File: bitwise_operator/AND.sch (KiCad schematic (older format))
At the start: 4 parts, among them U1 74LS08, U2 74LS08, U3 74LS08, U4 74LS08

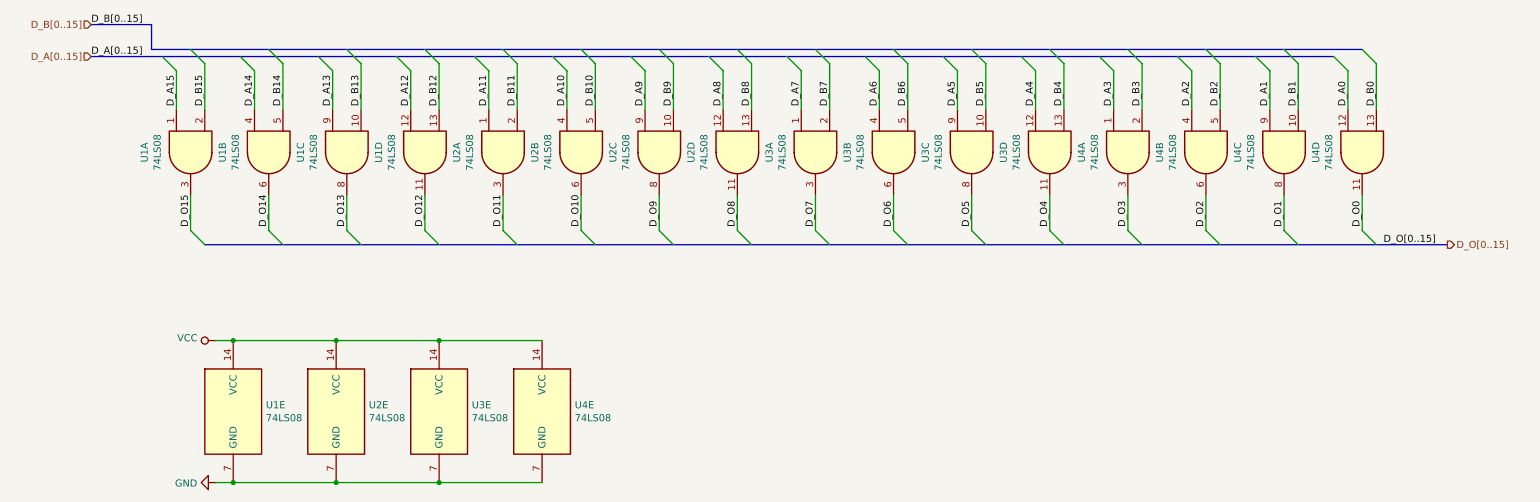
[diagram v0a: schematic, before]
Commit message: add bit operations
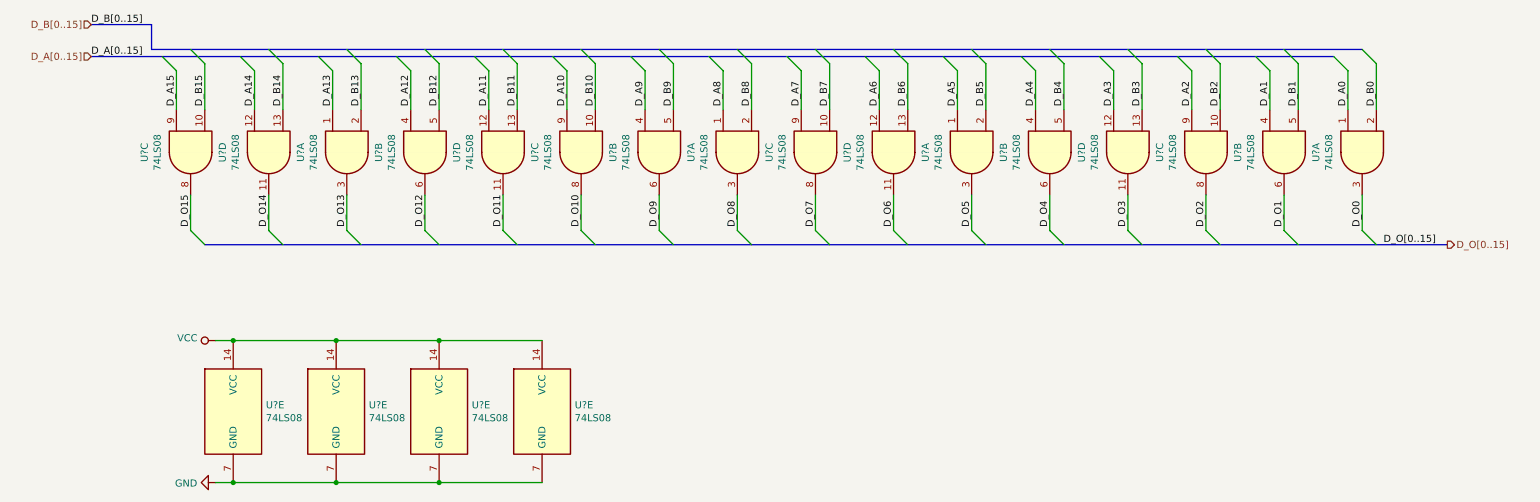
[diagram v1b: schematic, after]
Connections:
- net D_A0: now also U4.1; no longer U4.12
- net D_A1: now also U4.4; no longer U4.9
- net D_A10: now also U2.9; no longer U2.4
- net D_A11: now also U2.12; no longer U2.1
- net D_A12: now also U1.4; no longer U1.12
- net D_A13: now also U1.1; no longer U1.9
- net D_A14: now also U1.12; no longer U1.4
- net D_A15: now also U1.9; no longer U1.1
- net D_A2: now also U4.9; no longer U4.4
- net D_A3: now also U4.12; no longer U4.1
- net D_A4: now also U3.4; no longer U3.12
- net D_A5: now also U3.1; no longer U3.9
- net D_A6: now also U3.12; no longer U3.4
- net D_A7: now also U3.9; no longer U3.1
- net D_A8: now also U2.1; no longer U2.12
- net D_A9: now also U2.4; no longer U2.9
- net D_B0: now also U4.2; no longer U4.13
- net D_B1: now also U4.5; no longer U4.10
- net D_B10: now also U2.10; no longer U2.5
- net D_B11: now also U2.13; no longer U2.2
- net D_B12: now also U1.5; no longer U1.13
- net D_B13: now also U1.2; no longer U1.10
- net D_B14: now also U1.13; no longer U1.5
- net D_B15: now also U1.10; no longer U1.2
- net D_B2: now also U4.10; no longer U4.5
- net D_B3: now also U4.13; no longer U4.2
- net D_B4: now also U3.5; no longer U3.13
- net D_B5: now also U3.2; no longer U3.10
- net D_B6: now also U3.13; no longer U3.5
- net D_B7: now also U3.10; no longer U3.2
- net D_B8: now also U2.2; no longer U2.13
- net D_B9: now also U2.5; no longer U2.10
- net D_O0: now also U4.3; no longer U4.11
- net D_O1: now also U4.6; no longer U4.8
- net D_O10: now also U2.8; no longer U2.6
- net D_O11: now also U2.11; no longer U2.3
- net D_O12: now also U1.6; no longer U1.11
- net D_O13: now also U1.3; no longer U1.8
- net D_O14: now also U1.11; no longer U1.6
- net D_O15: now also U1.8; no longer U1.3
- net D_O2: now also U4.8; no longer U4.6
- net D_O3: now also U4.11; no longer U4.3
- net D_O4: now also U3.6; no longer U3.11
- net D_O5: now also U3.3; no longer U3.8
- net D_O6: now also U3.11; no longer U3.6
- net D_O7: now also U3.8; no longer U3.3
- net D_O8: now also U2.3; no longer U2.11
- net D_O9: now also U2.6; no longer U2.8

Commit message: part lists
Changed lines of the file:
@@
 EESchema Schematic File Version 4
-LIBS:computer-cache
+LIBS:bitwise_operator_pcb-cache
 EELAYER 30 0
 EELAYER END
 $Descr A4 11693 8268
 encoding utf-8
-Sheet 3 36
+Sheet 3 13
 Title ""
 Date ""
@@
 AR Path="/5F0D7DA0/5F2E31C3/5F2EF324" Ref="U1"  Part="3"
 AR Path="/5F0D7DA0/5F35ADA4/5F2EF324" Ref="U?"  Part="1"
-F 0 "U?" H 1775 3250 50  0000 C CNN
+F 0 "U1" H 1775 3250 50  0000 C CNN
 F 1 "74LS08" H 1775 3159 50  0000 C CNN
 F 2 "Package_DIP:DIP-14_W7.62mm_LongPads" H 1775 2925 50  0001 C CNN
@@
 AR Path="/5F0D7DA0/5F2E31C3/5F2EF32A" Ref="U1"  Part="4"
 AR Path="/5F0D7DA0/5F35ADA4/5F2EF32A" Ref="U?"  Part="2"
-F 0 "U?" H 2325 3250 50  0000 C CNN
+F 0 "U1" H 2325 3250 50  0000 C CNN
 F 1 "74LS08" H 2325 3159 50  0000 C CNN
 F 2 "Package_DIP:DIP-14_W7.62mm_LongPads" H 2325 2925 50  0001 C CNN
@@
 AR Path="/5F0D7DA0/5F2E31C3/5F2EF330" Ref="U1"  Part="1"
 AR Path="/5F0D7DA0/5F35ADA4/5F2EF330" Ref="U?"  Part="3"
-F 0 "U?" H 2875 3250 50  0000 C CNN
+F 0 "U1" H 2875 3250 50  0000 C CNN
 F 1 "74LS08" H 2875 3159 50  0000 C CNN
 F 2 "Package_DIP:DIP-14_W7.62mm_LongPads" H 2875 2925 50  0001 C CNN
@@
 AR Path="/5F0D7DA0/5F2E31C3/5F2EF336" Ref="U1"  Part="2"
 AR Path="/5F0D7DA0/5F35ADA4/5F2EF336" Ref="U?"  Part="4"
-F 0 "U?" H 3425 3250 50  0000 C CNN
+F 0 "U1" H 3425 3250 50  0000 C CNN
 F 1 "74LS08" H 3425 3159 50  0000 C CNN
 F 2 "Package_DIP:DIP-14_W7.62mm_LongPads" H 3425 2925 50  0001 C CNN
@@
 AR Path="/5F0D7DA0/5F2E31C3/5F2EF33C" Ref="U2"  Part="4"
 AR Path="/5F0D7DA0/5F35ADA4/5F2EF33C" Ref="U?"  Part="1"
-F 0 "U?" H 3975 3250 50  0000 C CNN
+F 0 "U2" H 3975 3250 50  0000 C CNN
 F 1 "74LS08" H 3975 3159 50  0000 C CNN
 F 2 "Package_DIP:DIP-14_W7.62mm_LongPads" H 3975 2925 50  0001 C CNN
@@
 AR Path="/5F0D7DA0/5F2E31C3/5F2EF342" Ref="U2"  Part="3"
 AR Path="/5F0D7DA0/5F35ADA4/5F2EF342" Ref="U?"  Part="2"
-F 0 "U?" H 4525 3250 50  0000 C CNN
+F 0 "U2" H 4525 3250 50  0000 C CNN
 F 1 "74LS08" H 4525 3159 50  0000 C CNN
 F 2 "Package_DIP:DIP-14_W7.62mm_LongPads" H 4525 2925 50  0001 C CNN
@@
 AR Path="/5F0D7DA0/5F2E31C3/5F2EF348" Ref="U2"  Part="2"
 AR Path="/5F0D7DA0/5F35ADA4/5F2EF348" Ref="U?"  Part="3"
-F 0 "U?" H 5075 3250 50  0000 C CNN
+F 0 "U2" H 5075 3250 50  0000 C CNN
 F 1 "74LS08" H 5075 3159 50  0000 C CNN
 F 2 "Package_DIP:DIP-14_W7.62mm_LongPads" H 5075 2925 50  0001 C CNN
@@
 AR Path="/5F0D7DA0/5F2E31C3/5F2EF34E" Ref="U2"  Part="1"
 AR Path="/5F0D7DA0/5F35ADA4/5F2EF34E" Ref="U?"  Part="4"
-F 0 "U?" H 5625 3250 50  0000 C CNN
+F 0 "U2" H 5625 3250 50  0000 C CNN
 F 1 "74LS08" H 5625 3159 50  0000 C CNN
 F 2 "Package_DIP:DIP-14_W7.62mm_LongPads" H 5625 2925 50  0001 C CNN
@@
 AR Path="/5F0D7DA0/5F2E31C3/5F2EF354" Ref="U3"  Part="3"
 AR Path="/5F0D7DA0/5F35ADA4/5F2EF354" Ref="U?"  Part="1"
-F 0 "U?" H 6175 3250 50  0000 C CNN
+F 0 "U3" H 6175 3250 50  0000 C CNN
 F 1 "74LS08" H 6175 3159 50  0000 C CNN
 F 2 "Package_DIP:DIP-14_W7.62mm_LongPads" H 6175 2925 50  0001 C CNN
@@
 AR Path="/5F0D7DA0/5F2E31C3/5F2EF35A" Ref="U3"  Part="4"
 AR Path="/5F0D7DA0/5F35ADA4/5F2EF35A" Ref="U?"  Part="2"
-F 0 "U?" H 6725 3250 50  0000 C CNN
+F 0 "U3" H 6725 3250 50  0000 C CNN
 F 1 "74LS08" H 6725 3159 50  0000 C CNN
 F 2 "Package_DIP:DIP-14_W7.62mm_LongPads" H 6725 2925 50  0001 C CNN
@@
 AR Path="/5F0D7DA0/5F2E31C3/5F2EF360" Ref="U3"  Part="1"
 AR Path="/5F0D7DA0/5F35ADA4/5F2EF360" Ref="U?"  Part="3"
-F 0 "U?" H 7275 3250 50  0000 C CNN
+F 0 "U3" H 7275 3250 50  0000 C CNN
 F 1 "74LS08" H 7275 3159 50  0000 C CNN
 F 2 "Package_DIP:DIP-14_W7.62mm_LongPads" H 7275 2925 50  0001 C CNN
@@
 AR Path="/5F0D7DA0/5F2E31C3/5F2EF366" Ref="U3"  Part="2"
 AR Path="/5F0D7DA0/5F35ADA4/5F2EF366" Ref="U?"  Part="4"
-F 0 "U?" H 7825 3250 50  0000 C CNN
+F 0 "U3" H 7825 3250 50  0000 C CNN
 F 1 "74LS08" H 7825 3159 50  0000 C CNN
 F 2 "Package_DIP:DIP-14_W7.62mm_LongPads" H 7825 2925 50  0001 C CNN
@@
 AR Path="/5F0D7DA0/5F2E31C3/5F2EF36C" Ref="U4"  Part="4"
 AR Path="/5F0D7DA0/5F35ADA4/5F2EF36C" Ref="U?"  Part="1"
-F 0 "U?" H 8375 3250 50  0000 C CNN
+F 0 "U4" H 8375 3250 50  0000 C CNN
 F 1 "74LS08" H 8375 3159 50  0000 C CNN
 F 2 "Package_DIP:DIP-14_W7.62mm_LongPads" H 8375 2925 50  0001 C CNN
@@
 AR Path="/5F0D7DA0/5F2E31C3/5F2EF372" Ref="U4"  Part="3"
 AR Path="/5F0D7DA0/5F35ADA4/5F2EF372" Ref="U?"  Part="2"
-F 0 "U?" H 8925 3250 50  0000 C CNN
+F 0 "U4" H 8925 3250 50  0000 C CNN
 F 1 "74LS08" H 8925 3159 50  0000 C CNN
 F 2 "Package_DIP:DIP-14_W7.62mm_LongPads" H 8925 2925 50  0001 C CNN
@@
 AR Path="/5F0D7DA0/5F2E31C3/5F2EF378" Ref="U4"  Part="2"
 AR Path="/5F0D7DA0/5F35ADA4/5F2EF378" Ref="U?"  Part="3"
-F 0 "U?" H 9475 3250 50  0000 C CNN
+F 0 "U4" H 9475 3250 50  0000 C CNN
 F 1 "74LS08" H 9475 3159 50  0000 C CNN
 F 2 "Package_DIP:DIP-14_W7.62mm_LongPads" H 9475 2925 50  0001 C CNN
@@
 AR Path="/5F0D7DA0/5F2E31C3/5F2EF37E" Ref="U4"  Part="1"
 AR Path="/5F0D7DA0/5F35ADA4/5F2EF37E" Ref="U?"  Part="4"
-F 0 "U?" H 10025 3250 50  0000 C CNN
+F 0 "U4" H 10025 3250 50  0000 C CNN
 F 1 "74LS08" H 10025 3159 50  0000 C CNN
 F 2 "Package_DIP:DIP-14_W7.62mm_LongPads" H 10025 2925 50  0001 C CNN
@@
 AR Path="/5F0D7DA0/5F2E31C3/5F302CAD" Ref="U1"  Part="5"
 AR Path="/5F0D7DA0/5F35ADA4/5F302CAD" Ref="U?"  Part="5"
-F 0 "U?" H 2305 4796 50  0000 L CNN
+F 0 "U1" H 2305 4796 50  0000 L CNN
 F 1 "74LS08" H 2305 4705 50  0000 L CNN
 F 2 "Package_DIP:DIP-14_W7.62mm_LongPads" H 2075 4750 50  0001 C CNN
@@
 AR Path="/5F0D7DA0/5F2E31C3/5F302CB3" Ref="U2"  Part="5"
 AR Path="/5F0D7DA0/5F35ADA4/5F302CB3" Ref="U?"  Part="5"
-F 0 "U?" H 3030 4796 50  0000 L CNN
+F 0 "U2" H 3030 4796 50  0000 L CNN
 F 1 "74LS08" H 3030 4705 50  0000 L CNN
 F 2 "Package_DIP:DIP-14_W7.62mm_LongPads" H 2800 4750 50  0001 C CNN
@@
 AR Path="/5F0D7DA0/5F2E31C3/5F302CBB" Ref="U3"  Part="5"
 AR Path="/5F0D7DA0/5F35ADA4/5F302CBB" Ref="U?"  Part="5"
-F 0 "U?" H 3755 4796 50  0000 L CNN
+F 0 "U3" H 3755 4796 50  0000 L CNN
 F 1 "74LS08" H 3755 4705 50  0000 L CNN
 F 2 "Package_DIP:DIP-14_W7.62mm_LongPads" H 3525 4750 50  0001 C CNN
@@
 AR Path="/5F0D7DA0/5F2E31C3/5F302CC3" Ref="U4"  Part="5"
 AR Path="/5F0D7DA0/5F35ADA4/5F302CC3" Ref="U?"  Part="5"
-F 0 "U?" H 4480 4796 50  0000 L CNN
+F 0 "U4" H 4480 4796 50  0000 L CNN
 F 1 "74LS08" H 4480 4705 50  0000 L CNN
 F 2 "Package_DIP:DIP-14_W7.62mm_LongPads" H 4250 4750 50  0001 C CNN
@@
 AR Path="/5F0D7DA0/5F2E31C3/5F649588" Ref="#PWR0103"  Part="1"
 AR Path="/5F0D7DA0/5F35ADA4/5F649588" Ref="#PWR?"  Part="1"
-F 0 "#PWR?" H 1950 4100 50  0001 C CNN
+F 0 "#PWR0103" H 1950 4100 50  0001 C CNN
 F 1 "VCC" V 1968 4377 50  0000 L CNN
 F 2 "" H 1950 4250 50  0001 C CNN
@@
 AR Path="/5F0D7DA0/5F2E31C3/5F64958B" Ref="#PWR0104"  Part="1"
 AR Path="/5F0D7DA0/5F35ADA4/5F64958B" Ref="#PWR?"  Part="1"
-F 0 "#PWR?" H 1950 5000 50  0001 C CNN
+F 0 "#PWR0104" H 1950 5000 50  0001 C CNN
 F 1 "GND" V 1955 5122 50  0000 R CNN
 F 2 "" H 1950 5250 50  0001 C CNN
